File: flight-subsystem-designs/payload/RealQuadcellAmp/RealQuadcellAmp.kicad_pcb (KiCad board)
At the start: 2 copper layers, 109.8 x 90.5 mm, 91 parts, among them J1 Screw_Terminal_01x02, J2 Conn_01x04_Pin, J3 Conn_01x04_Pin, U1 OPA1642AID, U2 OPA1642AID, U3 OPA1642AID, U4 OPA1642AID, U6 L78L33_SOT89

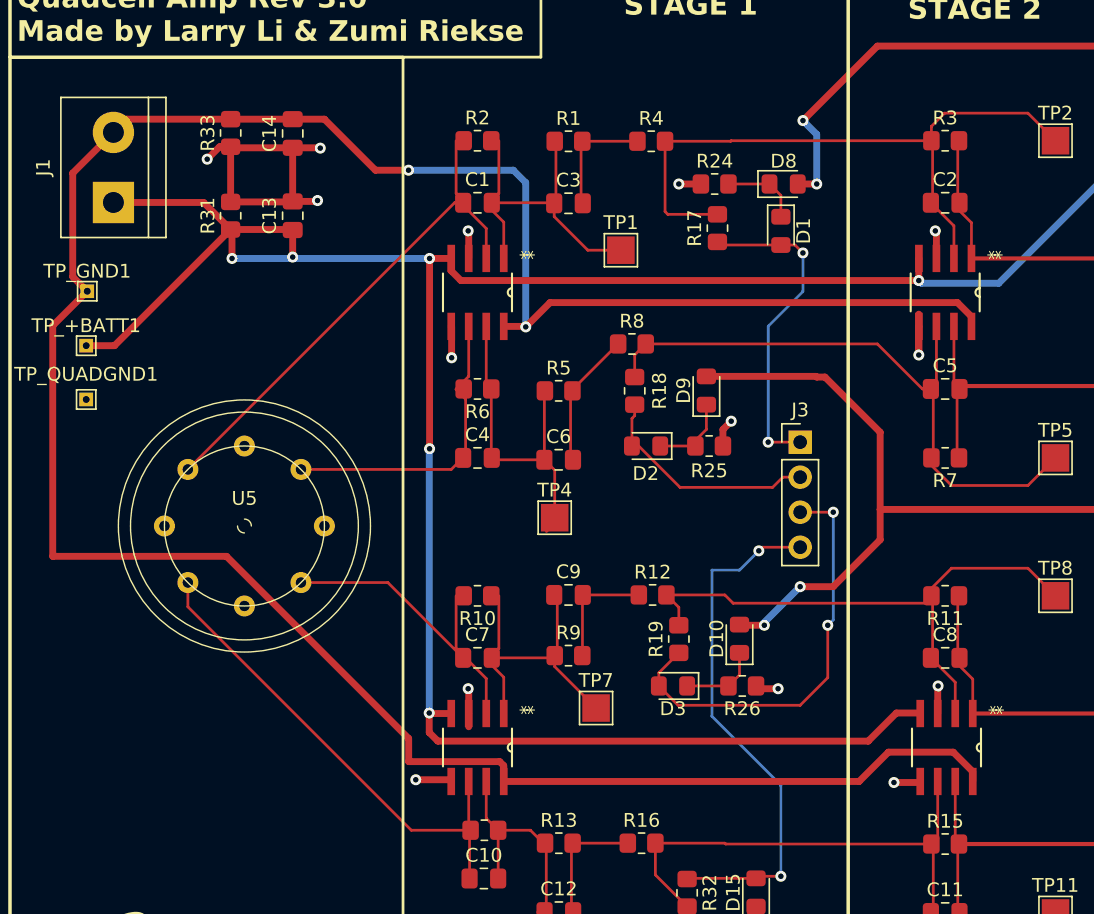
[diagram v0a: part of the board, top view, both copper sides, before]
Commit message: feat added new op amps and fied voltage divider problem on qc board
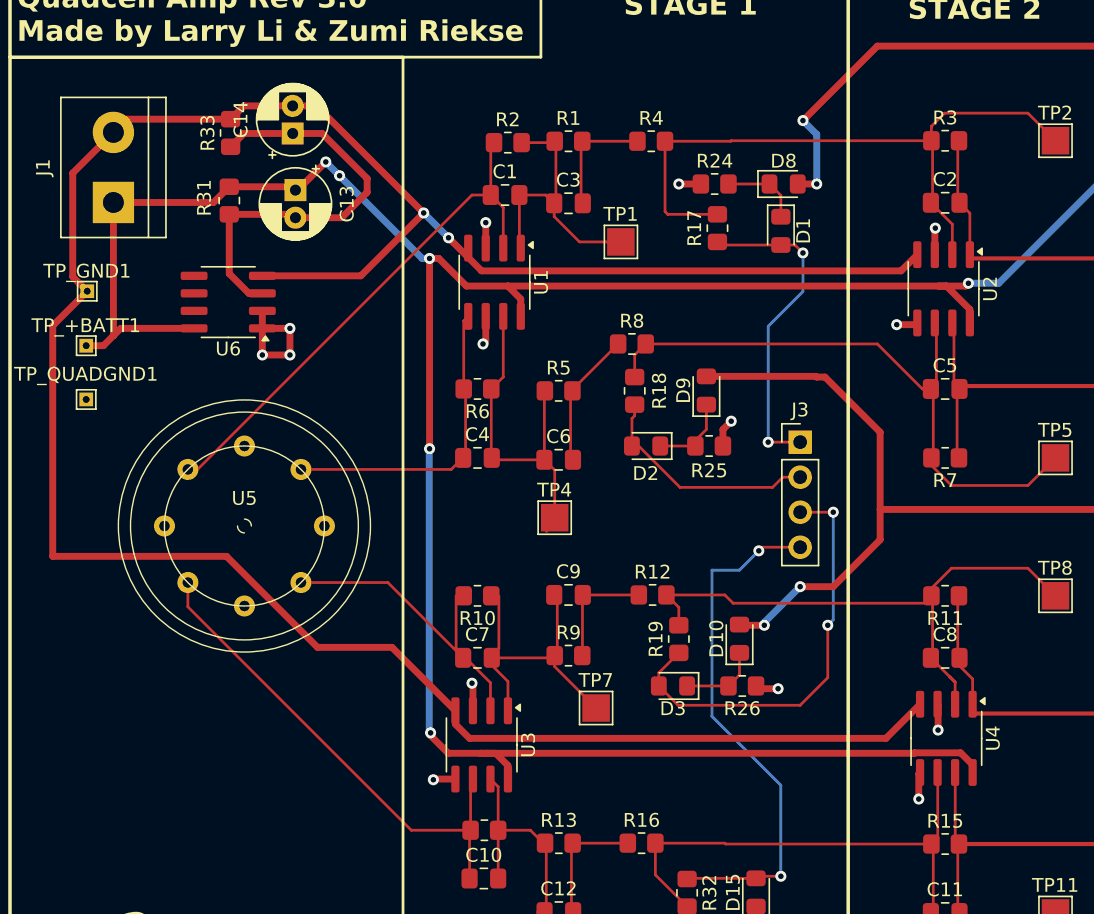
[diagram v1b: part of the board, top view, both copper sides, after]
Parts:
- added U6: LM2904, Package_SO:SOIC-8_3.9x4.9mm_P1.27mm, F.Cu at (101.3, 64.8)
- C13, C14: footprint Capacitor_SMD:C_0805_2012Metric_Pad1.18x1.45mm_HandSolder -> Capacitor_THT:CP_Radial_D5.0mm_P2.00mm
- U1, U2, U3, U4: value OPA1642AID -> LM2904; footprint OPA1642:D8 -> Package_SO:SOIC-8_3.9x4.9mm_P1.27mm
- moved R2 2.20 mm to (121.6, 53.2)
- moved C1 2.08 mm to (121.4, 57.0)
- moved C13 1.87 mm to (106.2, 56.6), turned to -90 degrees
- moved U1 1.44 mm to (120.6, 63.3)
- moved R31 1.10 mm to (101.4, 57.4), turned to -90 degrees
- moved U4 0.66 mm to (153.4, 96.4)
- moved TP1 0.60 mm to (129.8, 60.4)
- moved U3 0.36 mm to (119.7, 96.9)
- moved U2 0.29 mm to (153.2, 63.8)
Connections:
- C13 pad 2: QUAD_GND -> Net-(U6A-+)
- C14 pad 1: QUAD_GND -> Net-(U6A-+)
- R31 pad 2: QUAD_GND -> Net-(U6A-+)
- R33 pad 1: QUAD_GND -> Net-(U6A-+)
- U1 pad 4: VCC -> GND
- U1 pad 5: QUAD_GND -> /IN2
- U1 pad 6: /IN2 -> QUAD_GND
- U1 pad 8: GND -> VCC
- U2 pad 4: VCC -> GND
- U2 pad 8: GND -> VCC
- U3 pad 4: VCC -> GND
- U3 pad 8: GND -> VCC
- U4 pad 4: VCC -> GND
- U4 pad 8: GND -> VCC
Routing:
- net Net-(U6A-+): track 0.00 -> 30.9 mm
- net QUAD_GND: track 78.4 -> 54.2 mm
- net VCC: track 188.3 -> 197.1 mm
- net GND: track 189.4 -> 181.5 mm
- net Net-(C1-Pad2): track 25.1 -> 19.8 mm
- net Net-(C4-Pad2): track 24.5 -> 26.0 mm
- net /IN1: track 37.4 -> 38.3 mm
- net /STAGE2_OUT3: track 32.5 -> 31.8 mm
- net /IN2: track 22.5 -> 22.0 mm

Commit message: new quadcell rev
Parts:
- moved TP10 6.24 mm to (123.4, 106.4)
- moved C12 5.80 mm to (125.4, 103.2)
- moved C7 5.76 mm to (119.4, 84.8)
- moved D1 4.80 mm to (136.6, 59.4)
- moved R26 4.80 mm to (133.8, 92.8), turned to 0 degrees
- moved R10 4.66 mm to (119.4, 81.4)
- moved TP7 4.39 mm to (125.8, 90.4)
- moved C10 4.17 mm to (119.9, 102.4)
- moved D15 4.17 mm to (139.6, 103.4)
- moved D16 4.17 mm to (137.8, 108.0)
- moved R13 4.17 mm to (125.3, 99.8)
- moved R14 4.17 mm to (119.9, 98.9)
- moved R16 4.17 mm to (131.3, 99.8)
- moved R32 4.17 mm to (134.6, 103.4)
- moved R34 4.17 mm to (133.0, 108.0)
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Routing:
- net Net-(C7-Pad2): track 23.4 -> 8.38 mm
- net +3V3: track 235.2 -> 244.6 mm
- net VCC: track 197.1 -> 189.6 mm, vias 7 -> 5
- net /MOUT3: track 31.2 -> 24.7 mm
- net Net-(C4-Pad2): track 26.0 -> 19.6 mm
- net /MOUT4: track 38.2 -> 32.3 mm
- net GND: track 181.5 -> 176.2 mm
- net /STAGE1_OUT3: track 41.6 -> 37.8 mm
- net /STAGE1_OUT4: track 46.7 -> 43.3 mm
- net Net-(C9-Pad2): track 8.70 -> 5.36 mm
- net Net-(C10-Pad2): track 20.4 -> 17.4 mm
- net Net-(C6-Pad2): track 9.79 -> 7.03 mm
- net /STAGE2_OUT3: track 31.8 -> 34.3 mm
- net Net-(C3-Pad2): track 9.35 -> 6.92 mm
- net /STAGE1_OUT2: track 45.4 -> 47.7 mm
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
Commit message: fix: connected stage2
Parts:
- removed C15: 0.33u, Capacitor_SMD:C_0805_2012Metric_Pad1.18x1.45mm_HandSolder
- removed C16: 0.1u, Capacitor_SMD:C_0805_2012Metric_Pad1.18x1.45mm_HandSolder
- removed D1, D10, D11, D12, D13, D14, D15, D16, D2, D3, D4, D5, D6, D7, D8, D9: ~, Diode_SMD:D_0805_2012Metric_Pad1.15x1.40mm_HandSolder
- removed R17, R18, R19, R20, R21, R22, R23, R32: 1 kΩ, Resistor_SMD:R_0805_2012Metric_Pad1.20x1.40mm_HandSolder
- removed R24, R25, R26, R27, R28, R29, R30, R34: 40 Ω, Resistor_SMD:R_0805_2012Metric_Pad1.20x1.40mm_HandSolder
- removed the U6 at (173.8, 50.2)
- moved J2 35.3 mm to (153.5, 76.7)
- moved TP12 22.7 mm to (148.6, 103.0)
- moved TP9 22.7 mm to (148.6, 93.5)
- moved TP3 22.7 mm to (148.6, 61.5)
- moved TP6 22.7 mm to (148.6, 71.0)
- moved TP5 13.9 mm to (147.6, 78.2)
- moved C2 12.2 mm to (141.1, 57.8)
- moved C5 12.2 mm to (141.1, 71.3)
- moved R3 12.2 mm to (141.1, 53.3)
- moved R7 12.2 mm to (141.1, 76.3)
- moved TP2 12.2 mm to (149.1, 53.3)
- moved U2 12.2 mm to (141.0, 64.0)
- moved TP8 10.4 mm to (147.4, 86.2)
- moved TP11 9.12 mm to (148.7, 109.1)
- moved C11 7.99 mm to (141.8, 109.1)
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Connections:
- J2 pad 1: /FOUT1 -> /STAGE2_OUT1
- J2 pad 2: /FOUT2 -> /STAGE2_OUT2
- J2 pad 3: /FOUT3 -> /STAGE2_OUT3
- J2 pad 4: /FOUT4 -> /STAGE2_OUT4
- J3 pad 1: /MOUT1 -> /STAGE1_OUT1
- J3 pad 2: /MOUT2 -> /STAGE1_OUT2
- J3 pad 3: /MOUT3 -> /STAGE1_OUT3
- J3 pad 4: /MOUT4 -> /STAGE1_OUT4
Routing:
- net +3V3: track 244.6 -> 0.00 mm, vias 9 -> 0
- net VCC: track 189.6 -> 137.4 mm, vias 5 -> 3
- net /MOUT4: track 32.3 -> 0.00 mm, vias 2 -> 0
- net QUAD_GND: track 56.3 -> 24.0 mm, vias 20 -> 11
- net /FOUT4: track 28.9 -> 0.00 mm
- net /MOUT1: track 25.0 -> 0.00 mm, vias 2 -> 0
- net /MOUT3: track 24.7 -> 0.00 mm, vias 2 -> 0
- net /FOUT1: track 23.6 -> 0.00 mm
- net GND: track 176.2 -> 157.3 mm, vias 2 -> 4
- net /FOUT3: track 18.4 -> 0.00 mm
- net /MOUT2: track 17.4 -> 0.00 mm
- net /FOUT2: track 14.5 -> 0.00 mm
- net /STAGE1_OUT4: track 43.3 -> 54.7 mm, vias 0 -> 1
- net Net-(D13-K): track 8.74 -> 0.00 mm
- net Net-(D14-K): track 7.70 -> 0.00 mm
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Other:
- board size 109.8 x 90.5 mm -> 74.2 x 76.1 mm
- board text added: "Quadcell Amp Rev 4.0 Made by Larry Li & Zumi Riekse"
- board text removed: "It doesn't matter how beautiful your theory is, it doesn't matter how smart you are. If it doesn't agree with experiment, it's wrong. - Richard Feynman"
- board text removed: "OUTPUT"
- board text removed: "Quadcell Amp Rev 3.0 Made by Larry Li & Zumi Riekse"

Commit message: qc amp changes
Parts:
- added REF**: MountingHole_3.2mm_M3_DIN965_Pad, MountingHole:MountingHole_3.2mm_M3_DIN965_Pad, F.Cu at (88.8, 110.4)
- added REF**: MountingHole_3.2mm_M3_DIN965_Pad, MountingHole:MountingHole_3.2mm_M3_DIN965_Pad, F.Cu at (88.8, 44.0)
- added REF**: MountingHole_3.2mm_M3_DIN965_Pad, MountingHole:MountingHole_3.2mm_M3_DIN965_Pad, F.Cu at (154.2, 110.4)
- added REF**: MountingHole_3.2mm_M3_DIN965_Pad, MountingHole:MountingHole_3.2mm_M3_DIN965_Pad, F.Cu at (154.2, 44.0)
- moved TP11 1.68 mm to (147.0, 109.1)
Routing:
- net Net-(C7-Pad2): track 8.38 -> 16.0 mm
- net /STAGE1_OUT4: track 54.7 -> 53.0 mm
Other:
- board size 74.2 x 76.1 mm -> 75.6 x 76.1 mm
